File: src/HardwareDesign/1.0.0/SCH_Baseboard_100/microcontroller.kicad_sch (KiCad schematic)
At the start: 1 part, among them IC1 RP2354B

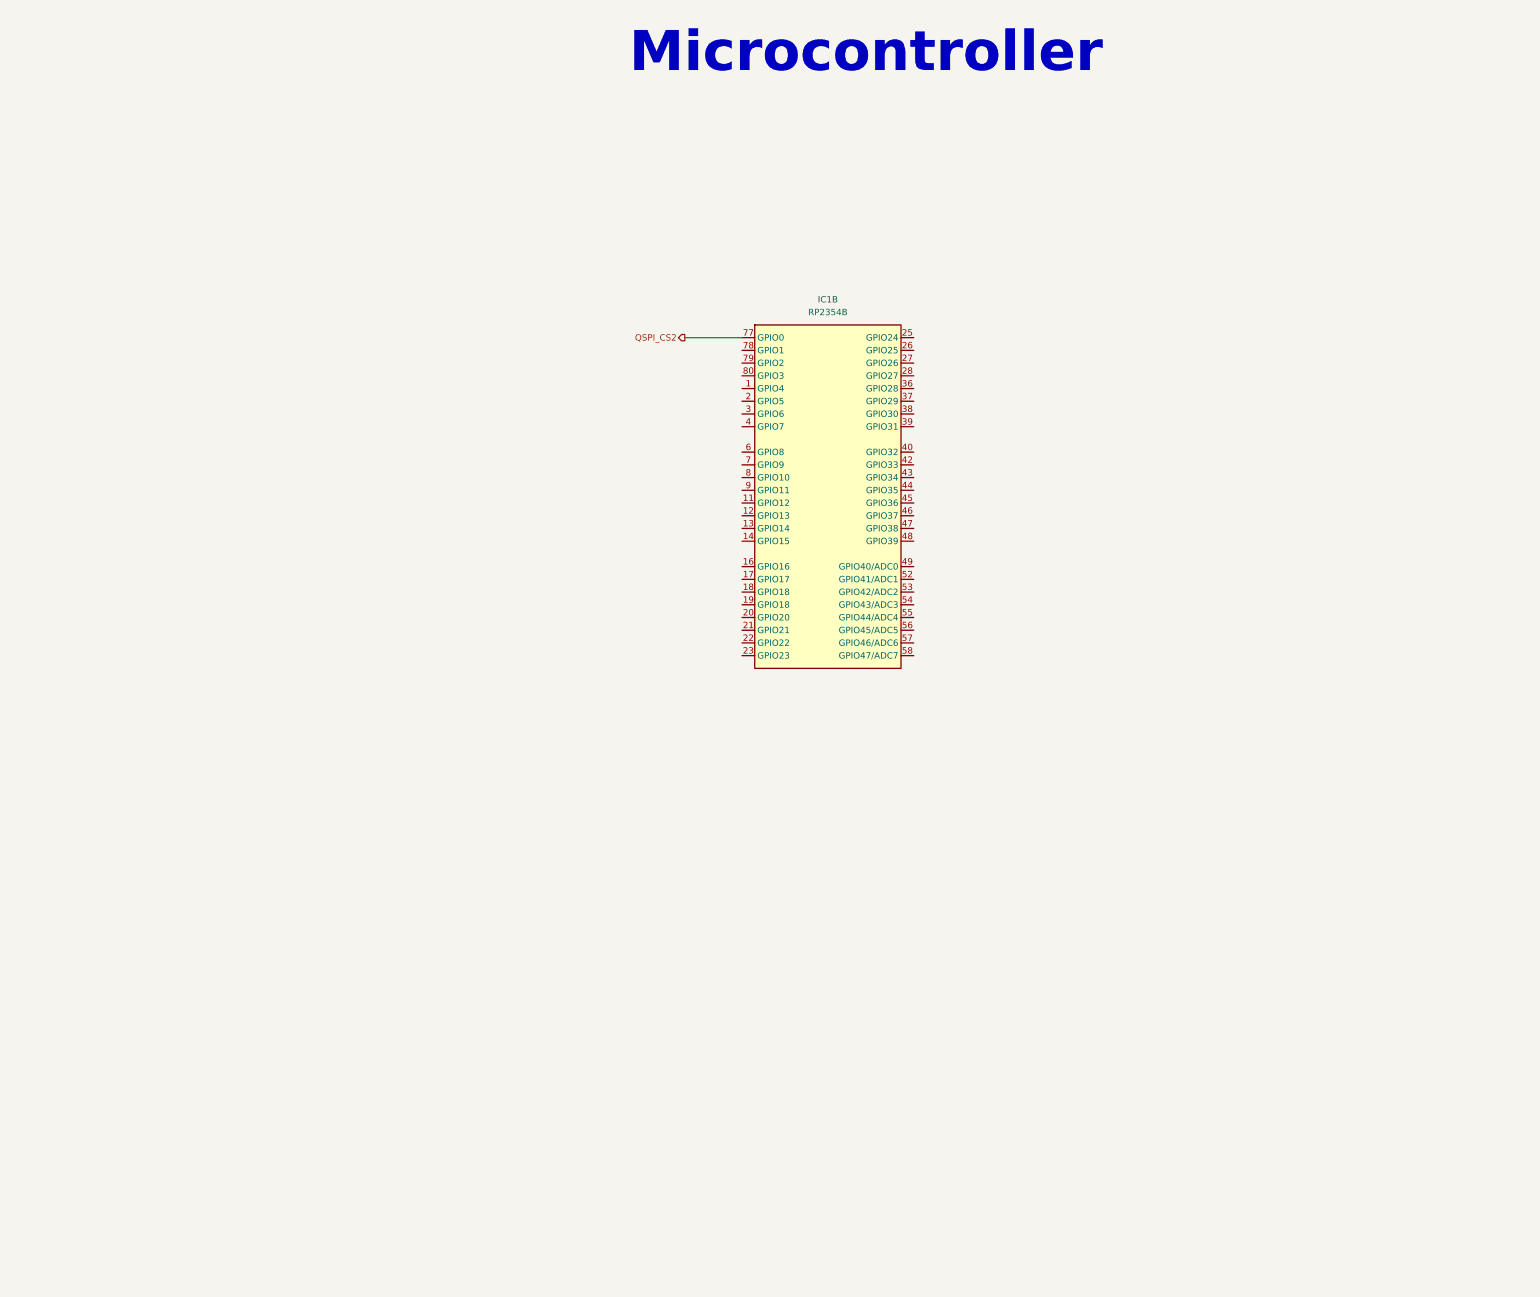
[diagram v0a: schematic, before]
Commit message: Add bladecore to design
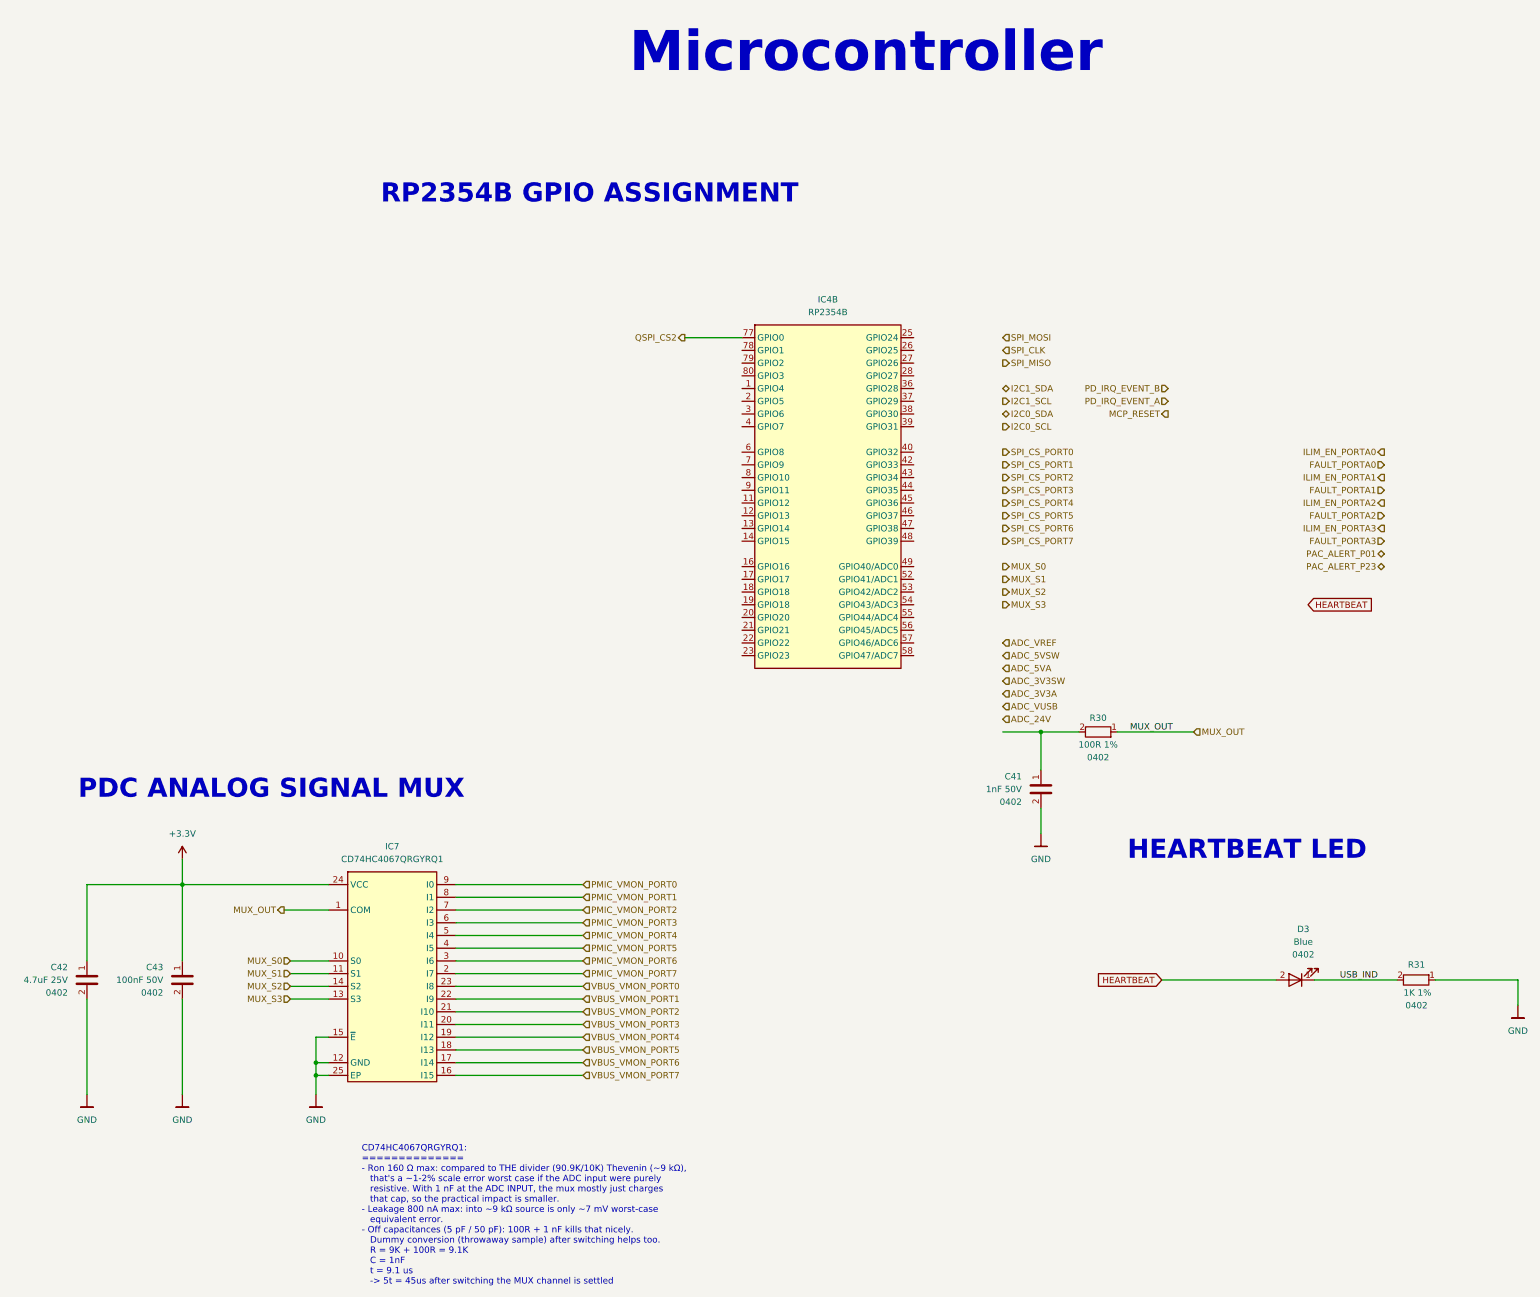
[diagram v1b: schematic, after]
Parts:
- added C41: 1nF 50V, Capacitor_SMD:C_0402_1005Metric, symbol DS_Capacitor_0402:1nF 50V 0402
- added C42: 4.7uF 25V, Capacitor_SMD:C_0402_1005Metric, symbol DS_Capacitor_0402:4.7uF 25V 0402
- added C43: 100nF 50V, Capacitor_SMD:C_0402_1005Metric, symbol DS_Capacitor_0402:100nF 50V 0402
- added D3: Blue, LED_SMD:LED_0402_1005Metric, symbol DS_Opto:Blue 0402
- added IC7: CD74HC4067QRGYRQ1, DS_Peripherals:Texas_RGY_R-PVQFN-N24_EP2.05x3.1mm_ThermalVias, symbol DS_Peripherals:CD74HC4067QRGYRQ1
- added R30: 100R 1%, Resistor_SMD:R_0402_1005Metric, symbol DS_Resistor_0402:100R 1% 0402
- added R31: 1K 1%, Resistor_SMD:R_0402_1005Metric, symbol DS_Resistor_0402:1K 1% 0402
- renumbered IC1 to IC4
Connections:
- new net: C41.1, R30.2
- new net +3.3V: C42.1, C43.1, IC7.24 (VCC)
- new net GND: C41.2, C42.2, C43.2, IC7.12 (GND), IC7.15 (~{E}), IC7.25 (EP), R31.1
- new net HEARTBEAT: D3.2
- new net MUX_OUT: IC7.1 (COM), R30.1
- new net MUX_S0: IC7.10 (S0)
- new net MUX_S1: IC7.11 (S1)
- new net MUX_S2: IC7.14 (S2)
- new net MUX_S3: IC7.13 (S3)
- new net PMIC_VMON_PORT0: IC7.9 (I0)
- new net PMIC_VMON_PORT1: IC7.8 (I1)
- new net PMIC_VMON_PORT2: IC7.7 (I2)
- new net PMIC_VMON_PORT3: IC7.6 (I3)
- new net PMIC_VMON_PORT4: IC7.5 (I4)
- new net PMIC_VMON_PORT5: IC7.4 (I5)
- new net PMIC_VMON_PORT6: IC7.3 (I6)
- new net PMIC_VMON_PORT7: IC7.2 (I7)
- new net USB_IND: D3.1, R31.2
- new net VBUS_VMON_PORT0: IC7.23 (I8)
- new net VBUS_VMON_PORT1: IC7.22 (I9)
- new net VBUS_VMON_PORT2: IC7.21 (I10)
- new net VBUS_VMON_PORT3: IC7.20 (I11)
- new net VBUS_VMON_PORT4: IC7.19 (I12)
- new net VBUS_VMON_PORT5: IC7.18 (I13)
- new net VBUS_VMON_PORT6: IC7.17 (I14)
- new net VBUS_VMON_PORT7: IC7.16 (I15)
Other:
- note added: "CD74HC4067QRGYRQ1: ============== - Ron 160 Ω max: compared to THE divider (90.9K/10K) Thevenin (~9 kΩ), that's a ~1-2% scale error worst case if the ADC input were purely resistive. With 1 nF at the ADC INPUT, the mux mostly just charges that cap, so the practical impact is smaller. - Leakage 800 nA max: into ~9 kΩ source is only ~7 mV worst-case equivalent error. - Off capacitances (5 pF / 50 p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"
- note added: "HEARTBEAT LED"
- note added: "PDC ANALOG SIGNAL MUX"
- note added: "RP2354B GPIO ASSIGNMENT"
